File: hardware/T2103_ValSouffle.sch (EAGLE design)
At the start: 39 parts, among them IC1 LM317MB, Q1 IRFB4310ZPBF, T1 2N2222, U1 ATMEGA328P-PU, U2 SN74HC595N, X1 16Mhz

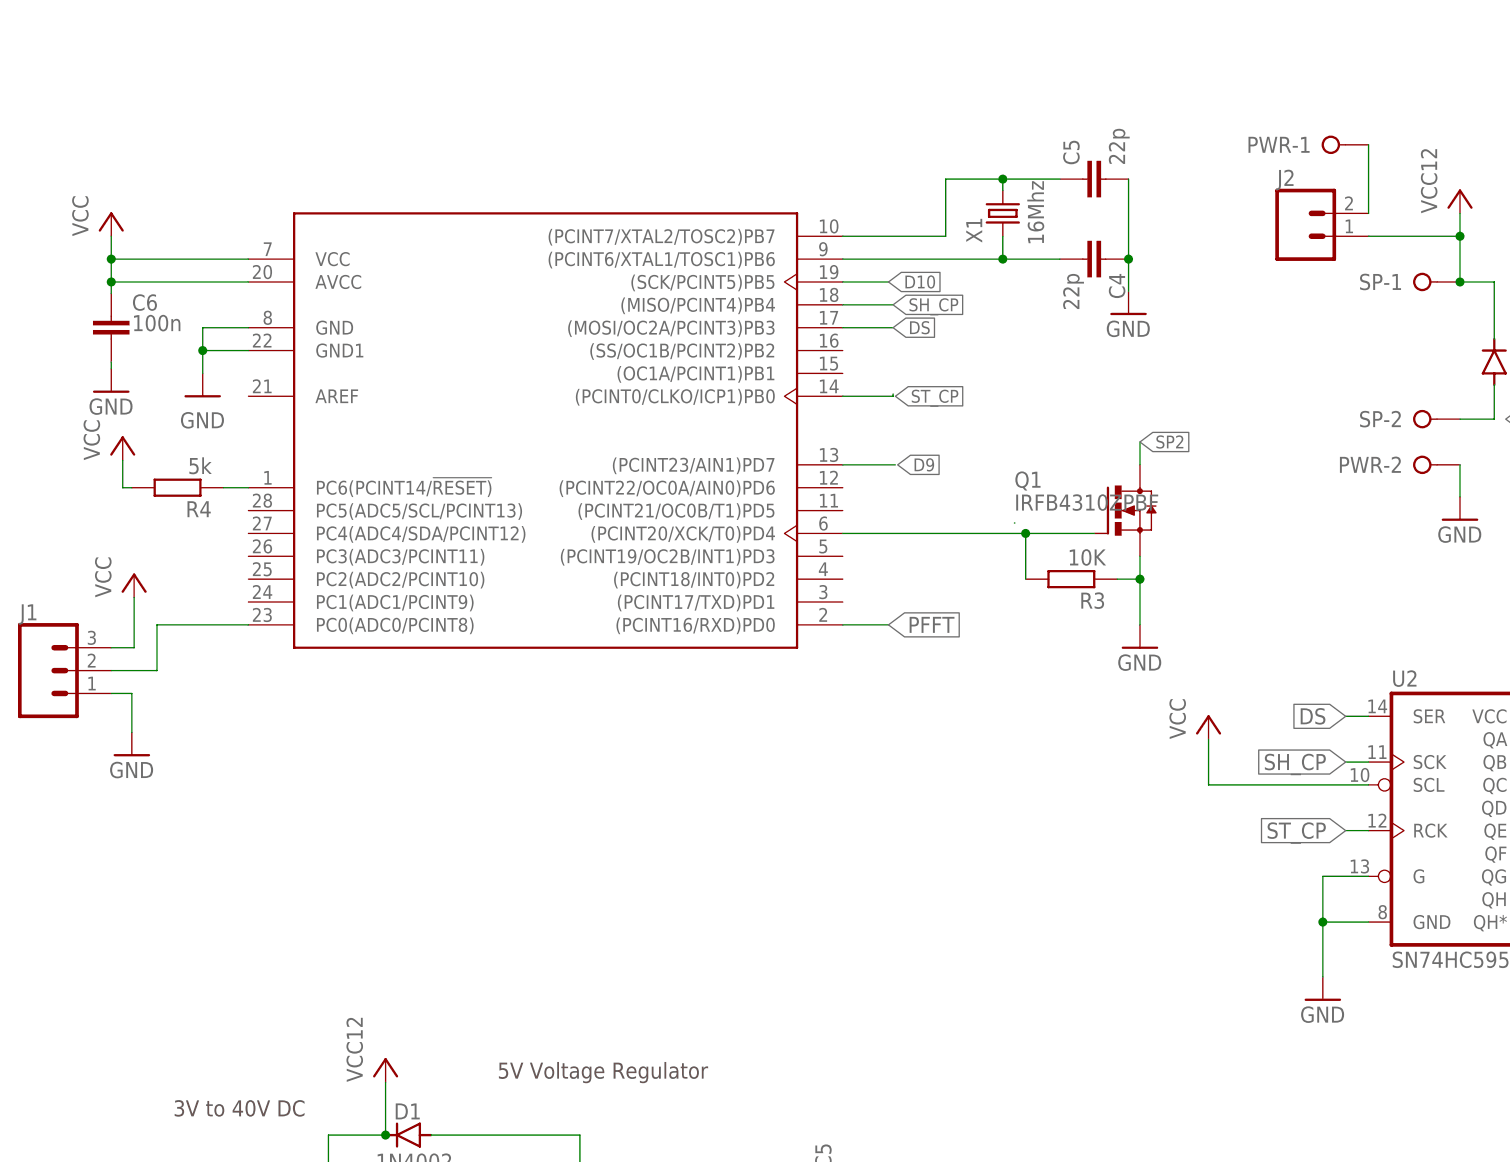
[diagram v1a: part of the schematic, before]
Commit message: Add manual switch
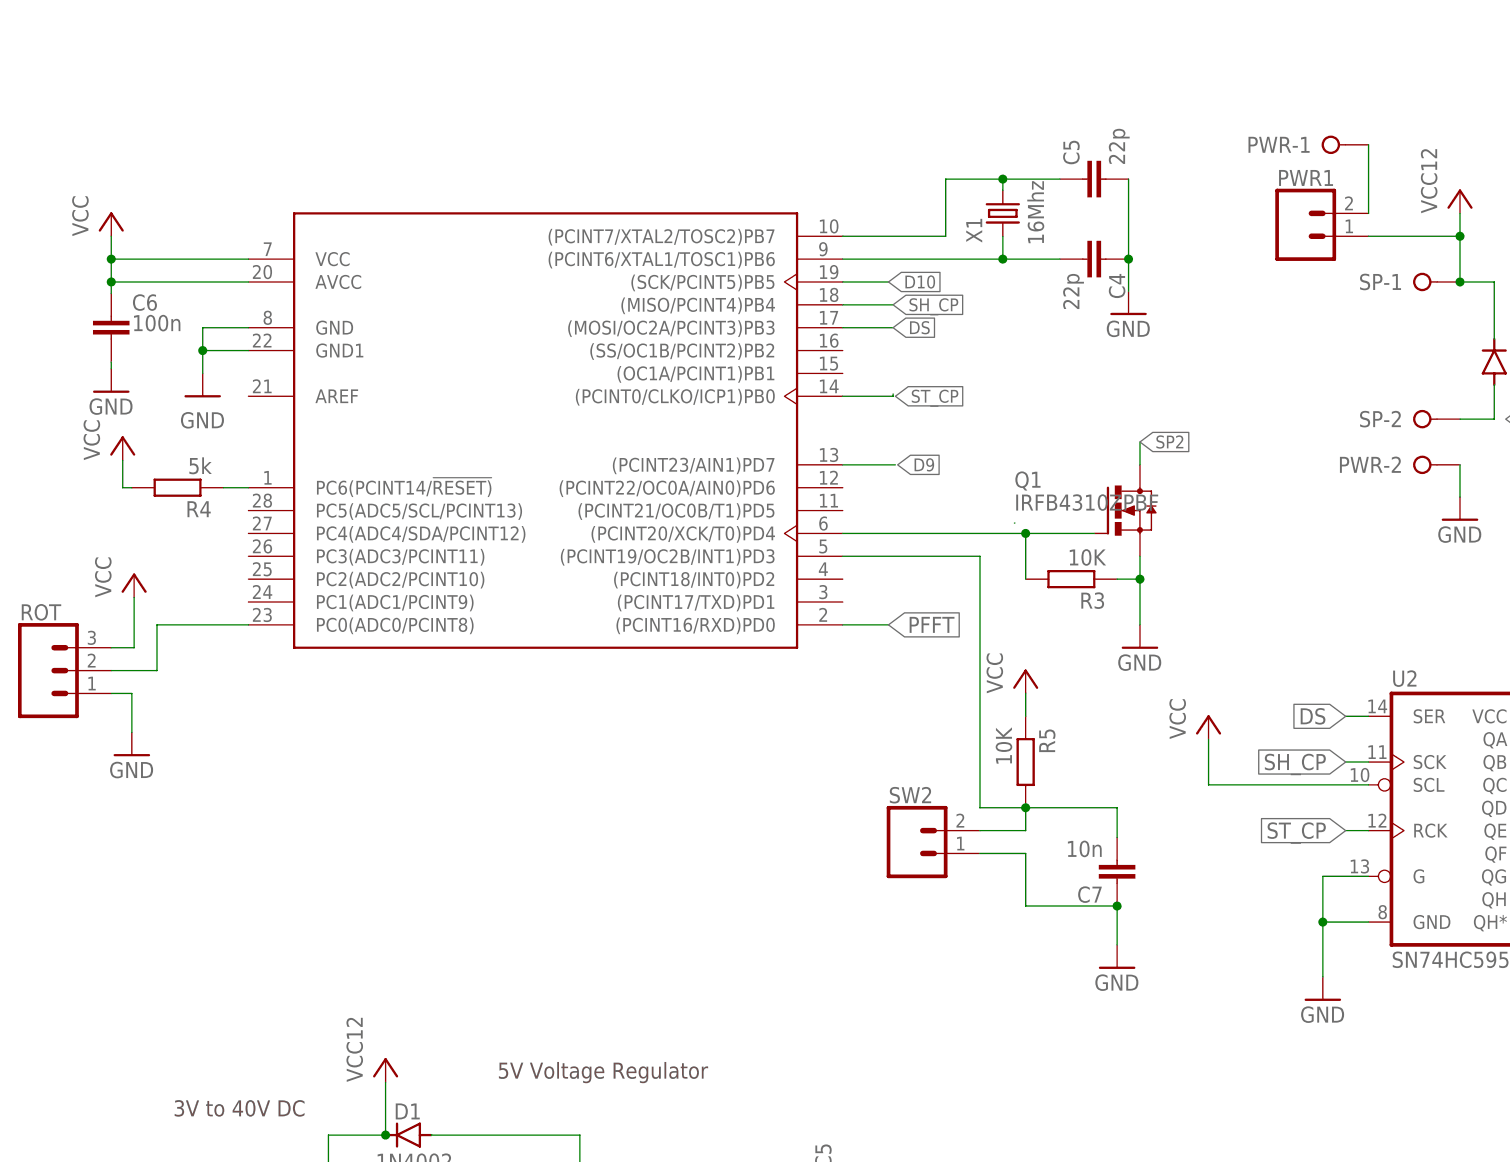
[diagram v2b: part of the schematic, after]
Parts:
- added C7: 10n, resistor:C-EU025-025X050
- added R5: 10K, resistor:R-EU_0207/10
- added SW2: (no value), SparkFun-Connectors:CONN_02
- renumbered J1 to ROT, J2 to PWR1
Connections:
- new net N$22: C7.2, R5.2, SW2.2, U1.(PCINT19/OC2B/INT1)PD3
- net GND: now also C7.1, SW2.1
- net VCC: now also R5.1
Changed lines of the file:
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@@
 <part name="SUPPLY8" library="supply1" library_urn="urn:adsk.eagle:library:371" deviceset="GND" device=""/>
 <part name="D3" library="diode" library_urn="urn:adsk.eagle:library:210" deviceset="1N4004" device="" package3d_urn="urn:adsk.eagle:package:43336/1" value="1N4002"/>
-<part name="J1" library="SparkFun-Connectors" library_urn="urn:adsk.eagle:library:513" deviceset="CONN_03" device="" package3d_urn="urn:adsk.eagle:package:38063/1"/>
+<part name="ROT" library="SparkFun-Connectors" library_urn="urn:adsk.eagle:library:513" deviceset="CONN_03" device="" package3d_urn="urn:adsk.eagle:package:38063/1"/>
 <part name="P+8" library="supply1" library_urn="urn:adsk.eagle:library:371" deviceset="VCC" device=""/>
 <part name="GND4" library="supply1" library_urn="urn:adsk.eagle:library:371" deviceset="GND" device=""/>
@@
 <part name="P+10" library="supply1" library_urn="urn:adsk.eagle:library:371" deviceset="VCC" device="" value="VCC5"/>
 <part name="SUPPLY10" library="supply1" library_urn="urn:adsk.eagle:library:371" deviceset="GND" device=""/>
-<part name="J2" library="SparkFun-Connectors" library_urn="urn:adsk.eagle:library:513" deviceset="CONN_02" device="" package3d_urn="urn:adsk.eagle:package:38039/1"/>
+<part name="PWR1" library="SparkFun-Connectors" library_urn="urn:adsk.eagle:library:513" deviceset="CONN_02" device="" package3d_urn="urn:adsk.eagle:package:38039/1"/>
+<part name="SUPPLY11" library="supply1" library_urn="urn:adsk.eagle:library:371" deviceset="GND" device=""/>
+<part name="P+11" library="supply1" library_urn="urn:adsk.eagle:library:371" deviceset="VCC" device=""/>
+<part name="R5" library="resistor" library_urn="urn:adsk.eagle:library:348" deviceset="R-EU_" device="0207/10" package3d_urn="urn:adsk.eagle:package:23491/2" value="10K"/>
+<part name="C7" library="resistor" library_urn="urn:adsk.eagle:library:348" deviceset="C-EU" device="025-025X050" package3d_urn="urn:adsk.eagle:package:23629/2" value="10n"/>
+<part name="SW2" library="SparkFun-Connectors" library_urn="urn:adsk.eagle:library:513" deviceset="CONN_02" device="" package3d_urn="urn:adsk.eagle:package:38039/1"/>
 </parts>
 <sheets>
@@
 <attribute name="VALUE" x="160.3314" y="173.34" size="1.778" layer="96"/>
 </instance>
-<instance part="J1" gate="J$1" x="-2.54" y="139.7" smashed="yes">
+<instance part="ROT" gate="J$1" x="-2.54" y="139.7" smashed="yes">
 <attribute name="VALUE" x="-5.08" y="132.334" size="1.778" layer="96" font="vector"/>
 <attribute name="NAME" x="-5.08" y="145.288" size="1.778" layer="95" font="vector"/>
@@
 <attribute name="VALUE" x="132.08" y="37.846" size="1.778" layer="96"/>
 </instance>
-<instance part="J2" gate="G$1" x="137.16" y="187.96" smashed="yes">
+<instance part="PWR1" gate="G$1" x="137.16" y="187.96" smashed="yes">
 <attribute name="VALUE" x="134.62" y="180.594" size="1.778" layer="96" font="vector"/>
 <attribute name="NAME" x="134.62" y="193.548" size="1.778" layer="95" font="vector"/>
+</instance>
+<instance part="SUPPLY11" gate="1" x="116.84" y="106.68" smashed="yes">
+<attribute name="VALUE" x="114.3" y="104.14" size="1.778" layer="96"/>
+</instance>
+<instance part="P+11" gate="VCC" x="106.68" y="139.7" smashed="yes">
+<attribute name="VALUE" x="104.14" y="137.16" size="1.778" layer="96" rot="R90"/>
+</instance>
+<instance part="R5" gate="G$1" x="106.68" y="129.54" smashed="yes" rot="R270">
+<attribute name="NAME" x="108.1786" y="133.35" size="1.778" layer="95" rot="R270"/>
+<attribute name="VALUE" x="103.378" y="133.35" size="1.778" layer="96" rot="R270"/>
+</instance>
+<instance part="C7" gate="G$1" x="116.84" y="116.078" smashed="yes" rot="R180">
+<attribute name="NAME" x="115.316" y="115.697" size="1.778" layer="95" rot="R180"/>
+<attribute name="VALUE" x="115.316" y="120.777" size="1.778" layer="96" rot="R180"/>
+</instance>
+<instance part="SW2" gate="G$1" x="93.98" y="119.38" smashed="yes">
+<attribute name="VALUE" x="91.44" y="112.014" size="1.778" layer="96" font="vector"/>
+<attribute name="NAME" x="91.44" y="124.968" size="1.778" layer="95" font="vector"/>
 </instance>
 </instances>
@@
 <segment>
 <pinref part="GND4" gate="1" pin="GND"/>
-<pinref part="J1" gate="J$1" pin="1"/>
+<pinref part="ROT" gate="J$1" pin="1"/>
 <wire x1="7.366" y1="132.842" x2="7.366" y2="137.16" width="0.1524" layer="91"/>
 <wire x1="7.366" y1="137.16" x2="5.08" y2="137.16" width="0.1524" layer="91"/>
@@
 <pinref part="SUPPLY10" gate="1" pin="GND"/>
 <wire x1="134.62" y1="48.26" x2="134.62" y2="42.926" width="0.1524" layer="91"/>
+</segment>
+<segment>
+<pinref part="C7" gate="G$1" pin="1"/>
+<pinref part="SUPPLY11" gate="1" pin="GND"/>
+<wire x1="116.84" y1="113.538" x2="116.84" y2="109.22" width="0.1524" layer="91"/>
+<wire x1="116.84" y1="113.538" x2="106.68" y2="113.538" width="0.1524" layer="91"/>
+<wire x1="106.68" y1="113.538" x2="106.68" y2="119.38" width="0.1524" layer="91"/>
+<junction x="116.84" y="113.538"/>
+<pinref part="SW2" gate="G$1" pin="1"/>
+<wire x1="101.6" y1="119.38" x2="106.68" y2="119.38" width="0.1524" layer="91"/>
 </segment>
 </net>
@@
 <pinref part="P+8" gate="VCC" pin="VCC"/>
 <wire x1="7.62" y1="147.828" x2="7.62" y2="142.24" width="0.1524" layer="91"/>
-<pinref part="J1" gate="J$1" pin="3"/>
+<pinref part="ROT" gate="J$1" pin="3"/>
 <wire x1="7.62" y1="142.24" x2="5.08" y2="142.24" width="0.1524" layer="91"/>
+</segment>
+<segment>
+<pinref part="P+11" gate="VCC" pin="VCC"/>
+<pinref part="R5" gate="G$1" pin="1"/>
+<wire x1="106.68" y1="137.16" x2="106.68" y2="134.62" width="0.1524" layer="91"/>
 </segment>
 </net>
@@
 </segment>
 <segment>
-<pinref part="J2" gate="G$1" pin="1"/>
+<pinref part="PWR1" gate="G$1" pin="1"/>
 <wire x1="144.78" y1="187.96" x2="154.94" y2="187.96" width="0.1524" layer="91"/>
 <pinref part="P+2" gate="VCC" pin="VCC"/>
@@
 <wire x1="20.32" y1="144.78" x2="10.16" y2="144.78" width="0.1524" layer="91"/>
 <wire x1="10.16" y1="144.78" x2="10.16" y2="139.7" width="0.1524" layer="91"/>
-<pinref part="J1" gate="J$1" pin="2"/>
+<pinref part="ROT" gate="J$1" pin="2"/>
 <wire x1="10.16" y1="139.7" x2="5.08" y2="139.7" width="0.1524" layer="91"/>
 </segment>
@@
 <net name="VCCSHUT" class="0">
 <segment>
-<pinref part="J2" gate="G$1" pin="2"/>
+<pinref part="PWR1" gate="G$1" pin="2"/>
 <pinref part="PWR" gate="-1" pin="KL"/>
 <wire x1="144.78" y1="190.5" x2="144.78" y2="198.12" width="0.1524" layer="91"/>
 </segment>
 </net>
+<net name="N$22" class="0">
+<segment>
+<pinref part="U1" gate="G$1" pin="(PCINT19/OC2B/INT1)PD3"/>
+<wire x1="86.36" y1="152.4" x2="101.6" y2="152.4" width="0.1524" layer="91"/>
+<wire x1="101.6" y1="152.4" x2="101.6" y2="124.46" width="0.1524" layer="91"/>
+<pinref part="R5" gate="G$1" pin="2"/>
+<wire x1="101.6" y1="124.46" x2="106.68" y2="124.46" width="0.1524" layer="91"/>
+<pinref part="C7" gate="G$1" pin="2"/>
+<wire x1="106.68" y1="124.46" x2="116.84" y2="124.46" width="0.1524" layer="91"/>
+<wire x1="116.84" y1="124.46" x2="116.84" y2="121.158" width="0.1524" layer="91"/>
+<junction x="106.68" y="124.46"/>
+<pinref part="SW2" gate="G$1" pin="2"/>
+<wire x1="101.6" y1="121.92" x2="106.68" y2="121.92" width="0.1524" layer="91"/>
+<wire x1="106.68" y1="121.92" x2="106.68" y2="124.46" width="0.1524" layer="91"/>
+</segment>
+</net>

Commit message: Hardware update
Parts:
- R1: value 240Ω -> 220
- R2: value 720Ω -> 649
- R4: value 5k -> 10K
- RL1, RL10, RL2, RL3, RL4, RL5, RL6, RL7, RL8: value (none) -> 220
- RL9: value (none) -> 200
- R_LED, R_LED3: value 68 -> 220
- R_LED1: value 68 -> 10K
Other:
- note added: "4.93V, 500mA"
- note removed: "5V, 500mA"
